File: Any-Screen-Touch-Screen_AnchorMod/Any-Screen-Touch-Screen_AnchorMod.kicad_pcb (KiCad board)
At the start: 2 copper layers, 40 parts, among them J1 Reset button, J2 Flash button, J3 Power Switch, J4 Battery Terminals, J5 LED1, J6 LED2, J7 LED3, J8 LED4, P1 USB_C_Plug_USB2.0, U1 ESP32-S3-WROOM-1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

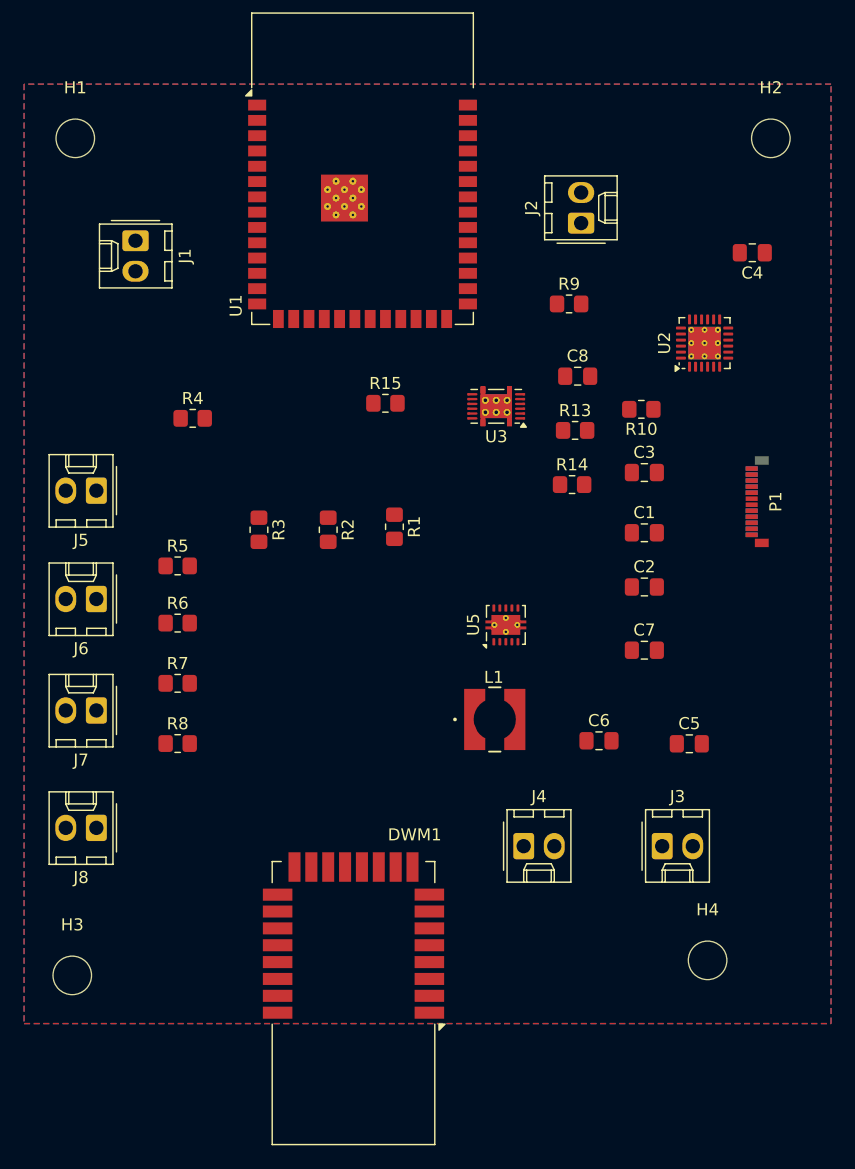
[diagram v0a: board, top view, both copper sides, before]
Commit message: did most of the PCB routing, updated lab notebook
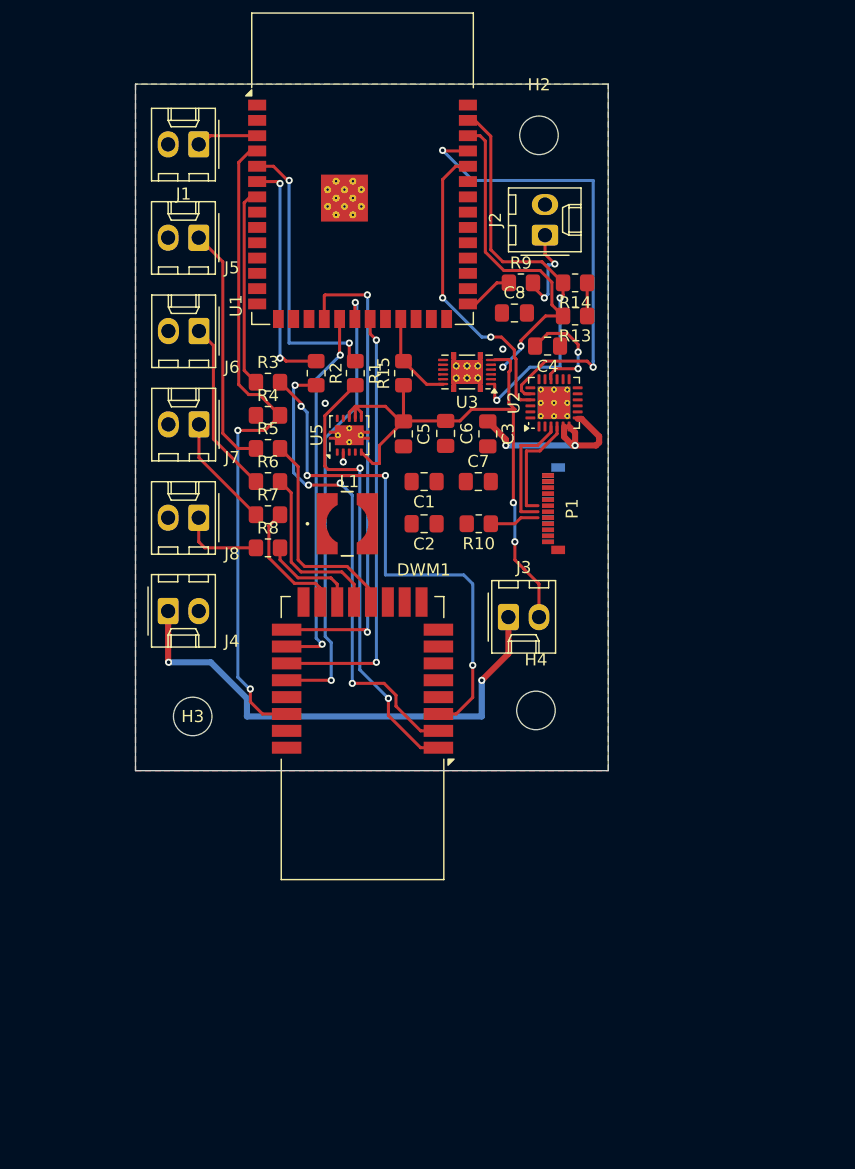
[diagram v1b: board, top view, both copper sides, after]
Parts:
- removed H1: MountingHole, MountingHole:MountingHole_3.2mm_M3
- moved J4 35.4 mm to (170.5, 86.0)
- moved C5 35.0 mm to (190.0, 71.3), turned to -90 degrees
- moved C6 28.5 mm to (193.5, 71.2), turned to 90 degrees
- moved J8 27.1 mm to (173.0, 78.2)
- moved J7 25.2 mm to (173.0, 70.5)
- moved H4 25.2 mm to (201.0, 94.2)
- moved J6 23.8 mm to (173.0, 62.8)
- moved H3 23.7 mm to (172.5, 94.8)
- moved J3 22.9 mm to (198.7, 86.5)
- moved J5 22.7 mm to (173.0, 55.0)
- moved DWM1 22.0 mm to (186.6, 96.5)
- moved U5 20.4 mm to (185.5, 71.4)
- moved L1 20.4 mm to (185.3, 78.8)
- moved C7 19.6 mm to (196.2, 75.2)
- moved H2 19.3 mm to (201.2, 46.5)
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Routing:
- net /INT: track 0.00 -> 55.3 mm, vias 0 -> 2
- net Net-(J3-Pin_2): track 0.00 -> 53.4 mm, vias 0 -> 2
- net Net-(DWM1-~{RST}): track 0.00 -> 43.8 mm, vias 0 -> 4
- net Net-(J3-Pin_1): track 0.00 -> 42.2 mm, vias 0 -> 2
- net /CS_AL: track 0.00 -> 40.3 mm, vias 0 -> 2
- net Net-(DWM1-WAKEUP): track 0.00 -> 39.8 mm, vias 0 -> 4
- net /USB_DATA_RXD: track 0.00 -> 39.4 mm, vias 0 -> 2
- net /SPI_CLK: track 0.00 -> 37.8 mm, vias 0 -> 2
- net Net-(DWM1-EXTON): track 0.00 -> 37.7 mm, vias 0 -> 2
- net /MISO: track 0.00 -> 36.2 mm, vias 0 -> 2
- net /I2C Data: track 0.00 -> 33.9 mm, vias 0 -> 2
- net /MOSI: track 0.00 -> 31.1 mm, vias 0 -> 2
- net /I2C Clock: track 0.00 -> 27.8 mm, vias 0 -> 2
- net /USB_DATA_TXD: track 0.00 -> 25.3 mm, vias 0 -> 2
- net /EXT_ON: track 0.00 -> 23.4 mm, vias 0 -> 2
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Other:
- board outline added: 39.2 x 57 mm

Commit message: update pcb
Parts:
- added H1: MountingHole, MountingHole:MountingHole_3.2mm_M3, F.Cu at (3.48, 3.48)
- moved U3 0.64 mm to (194.7, 66.0)
- turned C4 to 0 degrees
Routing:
- net +3.3V: track 17.2 -> 40.5 mm
- net GND: track 0.00 -> 18.2 mm, vias 2 -> 7
- net Net-(P1-VBUS-PadA4): track 0.00 -> 8.71 mm
- net Net-(U2-VPP): track 9.33 -> 6.79 mm
- net /I2C Data: track 33.9 -> 36.3 mm
- net /I2C Clock: track 27.8 -> 29.4 mm
- net Net-(DWM1-EXTON): track 37.7 -> 39.3 mm
- net /USB_D+: track 10.3 -> 11.3 mm
- net Net-(P1-CC): track 4.13 -> 4.96 mm
- net /USB_D-: track 9.26 -> 10.1 mm
- net Net-(J3-Pin_2): track 53.4 -> 54.1 mm
